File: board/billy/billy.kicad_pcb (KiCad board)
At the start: 2 copper layers, 70 x 50 mm, 82 parts, among them J1 Screw_Terminal_01x02, J10 Screw_Terminal_01x02, J11 Screw_Terminal_01x03, J12 USB_B_Micro, J2 Conn_01x06, J3 Screw_Terminal_01x02, J4 Screw_Terminal_01x02, J5 Conn_01x02, J6 Conn_01x03, J7 Screw_Terminal_01x06, Q1 AO3401A, Q2 AO3401A, Q4 AO3400A, Q6 AO3400A, Q7 AO3400A, SW1 TS-1088-AR02016, U1 ESP32-S3-WROOM-1, U2 DRV8833PWPR, U3 MAX98357A, U4 DRV8833PWPR, U5 LTC4412, U6 AP63203WU, U7 USBLC6-2SC6

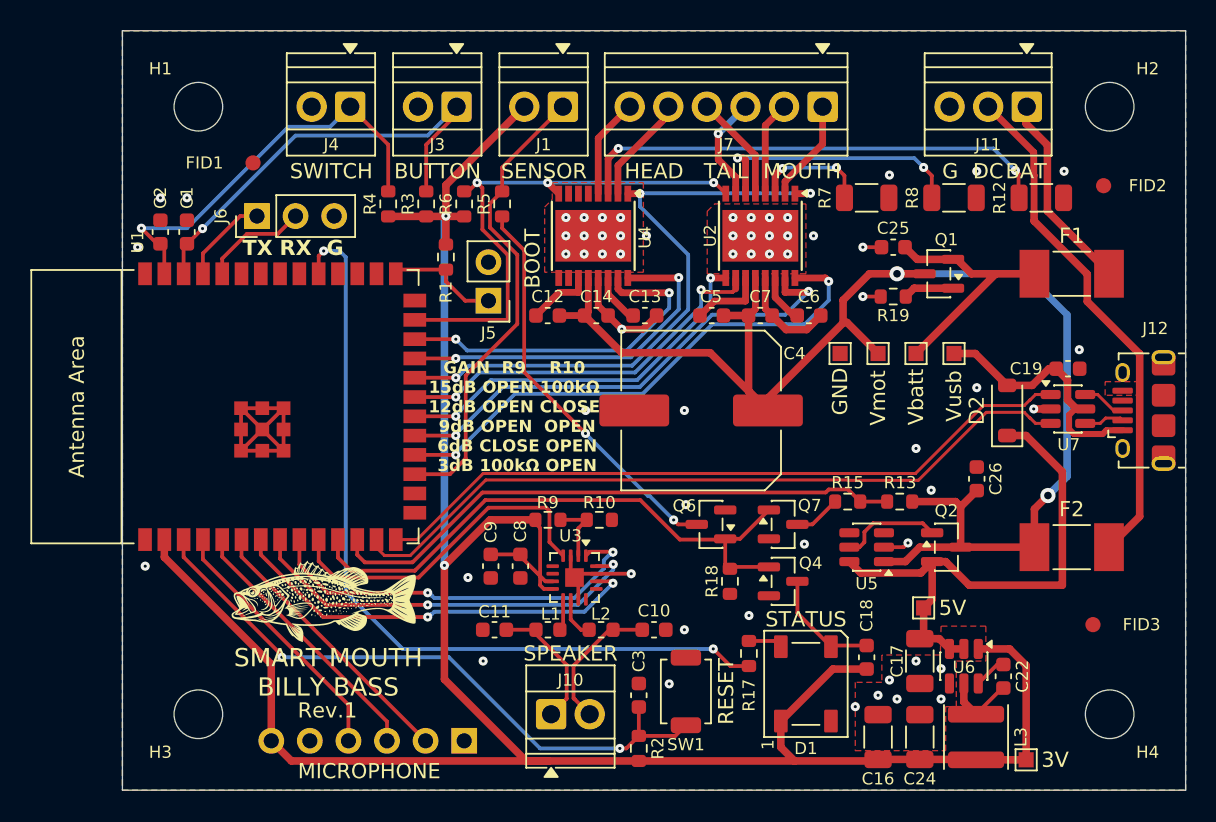
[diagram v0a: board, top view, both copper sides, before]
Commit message: Split rev.1's DRV8833 nSLEEP/nFAULT per chip for independent motor group control
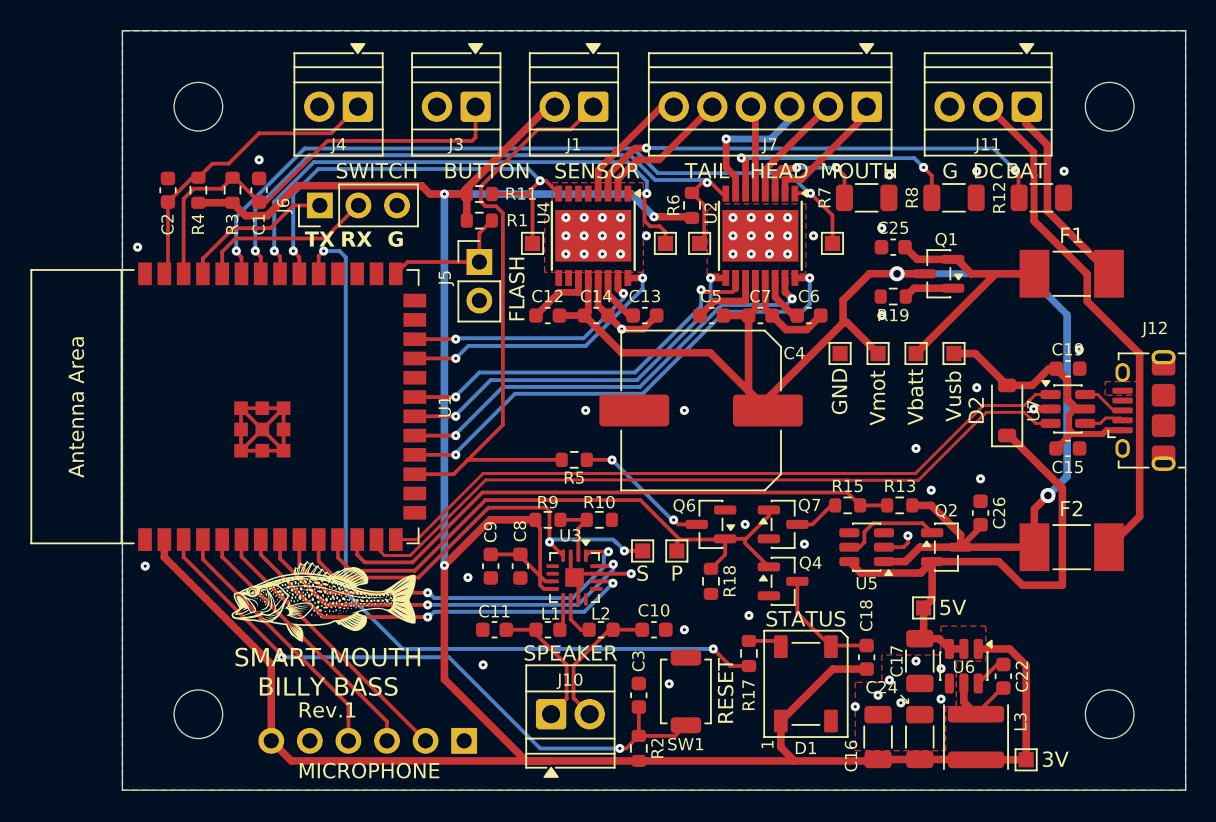
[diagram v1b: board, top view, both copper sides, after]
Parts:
- removed FID1, FID2, FID3: Fiducial_1mm_Mask2mm, Fiducial:Fiducial_1mm_Mask2mm
- added C15: 1u, Capacitor_SMD:C_0603_1608Metric, F.Cu at (212.2, 77.5)
- added R11: 10k, Resistor_SMD:R_0603_1608Metric, F.Cu at (173.5, 60.8)
- added TP10: TestPoint, TestPoint:TestPoint_Pad_1.0x1.0mm, F.Cu at (186.5, 84.2)
- added TP11: TestPoint, TestPoint:TestPoint_Pad_1.0x1.0mm, F.Cu at (185.8, 64.0)
- added TP12: TestPoint, TestPoint:TestPoint_Pad_1.0x1.0mm, F.Cu at (177.0, 64.0)
- added TP7: TestPoint, TestPoint:TestPoint_Pad_1.0x1.0mm, F.Cu at (196.8, 64.0)
- added TP8: TestPoint, TestPoint:TestPoint_Pad_1.0x1.0mm, F.Cu at (188.0, 64.0)
- added TP9: TestPoint, TestPoint:TestPoint_Pad_1.0x1.0mm, F.Cu at (184.2, 84.2)
- moved R5 17.5 mm to (179.8, 78.2), turned to 0 degrees
- moved R6 15.0 mm to (187.5, 61.5)
- moved R3 12.8 mm to (157.2, 60.5)
- moved R4 12.5 mm to (155.0, 60.5)
- moved C1 5.49 mm to (159.0, 60.5)
- moved J6 4.20 mm to (163.0, 61.5)
- moved R1 3.26 mm to (173.5, 62.5), turned to 0 degrees
- moved J7 2.90 mm to (199.0, 55.0)
- moved C2 2.80 mm to (153.0, 60.5)
- moved J5 2.62 mm to (173.5, 65.2), turned to 0 degrees
- moved C26 2.26 mm to (206.5, 81.8)
- moved J1 2.00 mm to (181.0, 55.0)
- moved J3 1.25 mm to (173.2, 55.0)
- moved R18 1.25 mm to (188.8, 86.2)
- moved J4 0.50 mm to (165.5, 55.0)
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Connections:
- net Vbatt renamed /Vbatt
- R6 pad 2: GPIO48 -> GPIO41
- U2 pad 1: GPIO14 -> GPIO42
- U2 pad 8: GPIO48 -> GPIO41
- U4 pad 1: GPIO14 -> GPIO40
- U4 pad 8: GPIO48 -> GPIO39
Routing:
- net GPIO42: track 0.00 -> 49.7 mm, vias 0 -> 2
- net GPIO41: track 0.00 -> 42.5 mm, vias 0 -> 2
- net GPIO14: track 41.9 -> 0.00 mm, vias 3 -> 0
- net GPIO40: track 0.00 -> 37.4 mm, vias 0 -> 2
- net GPIO48: track 34.5 -> 0.00 mm, vias 3 -> 0
- net GPIO39: track 0.00 -> 31.2 mm, vias 0 -> 2
- net +3.3V: track 159.0 -> 189.8 mm, vias 2 -> 3
- net Net-(Q6-D): track 26.4 -> 9.00 mm
- net GPIO9: track 30.7 -> 39.6 mm
- net GPIO1: track 26.8 -> 19.6 mm, vias 1 -> 0
- net GPIO47: track 23.4 -> 16.4 mm
- net GPIO17: track 22.4 -> 28.9 mm, vias 0 -> 2
- net GPIO21: track 24.2 -> 18.6 mm
- net U0RX: track 6.99 -> 11.6 mm
- net U0TX: track 5.92 -> 10.1 mm
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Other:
- board text added: "FLASH"
- board text added: "P"
- board text added: "S"
- board text removed: "BOOT"
- board text removed: "GAIN R9 R10 15dB OPEN 100kΩ 12dB OPEN CLOSE 9dB OPEN OPEN 6dB CLOSE OPEN 3dB 100kΩ OPEN"

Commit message: Split motor-rail bulk cap into two 220uF units, add solder-jumper Vmot->BUCK_IN bypass option
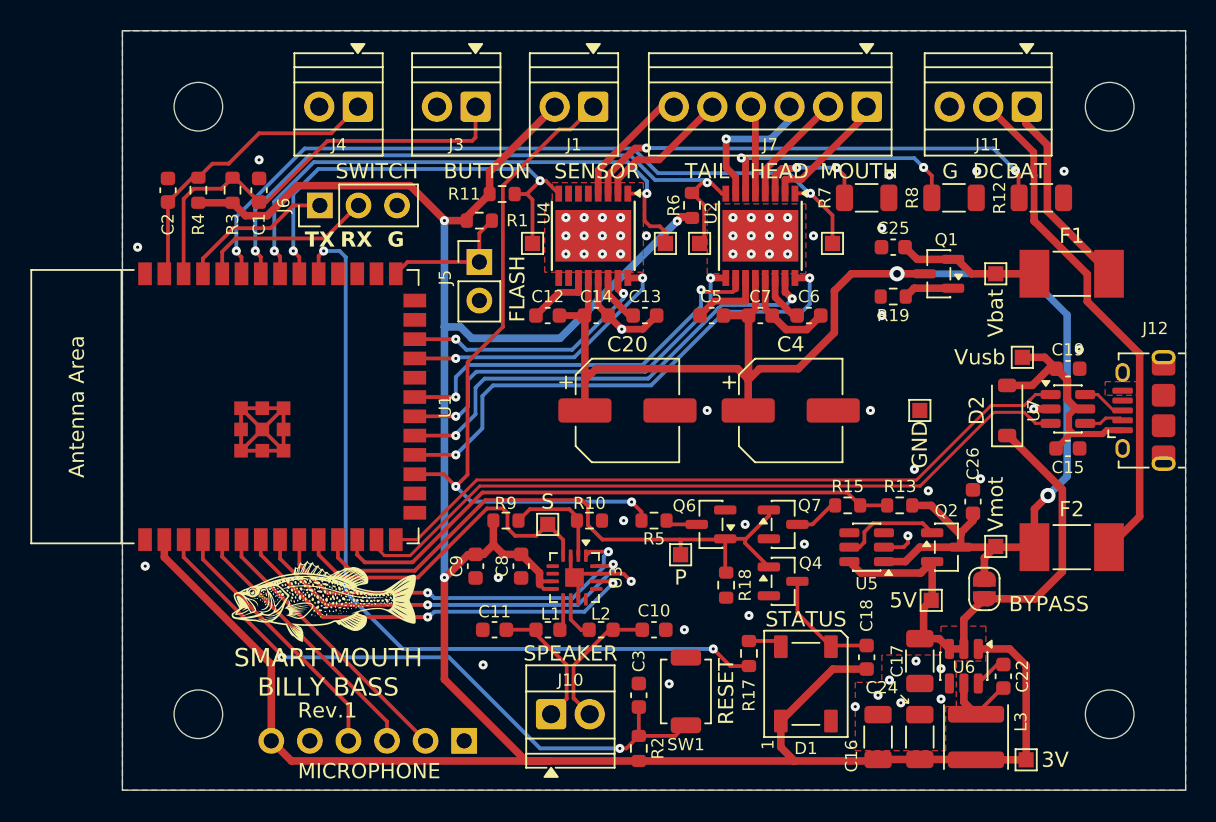
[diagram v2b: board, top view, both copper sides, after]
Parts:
- added C20: 220u, Capacitor_SMD:CP_Elec_6.3x5.9, F.Cu at (183.2, 75.0)
- added JP1: SolderJumper_2_Open, Jumper:SolderJumper-2_P1.3mm_Open_RoundedPad1.0x1.5mm, F.Cu at (206.8, 86.8)
- C4: value 1000u -> 220u; footprint Capacitor_SMD:C_Elec_10x10.2 -> Capacitor_SMD:CP_Elec_6.3x5.9
- moved TP1 14.9 mm to (207.5, 84.0)
- moved TP5 7.42 mm to (207.5, 66.0)
- moved R5 6.60 mm to (185.0, 82.2)
- moved TP9 6.49 mm to (178.0, 82.5)
- moved TP3 6.45 mm to (202.5, 75.0)
- moved C4 5.90 mm to (194.0, 75.0), turned to 0 degrees
- moved TP6 4.51 mm to (209.2, 71.5)
- moved R9 2.77 mm to (175.2, 82.2)
- moved R11 1.50 mm to (175.0, 60.8)
- moved R18 1.03 mm to (189.8, 86.5)
- moved C9 1.00 mm to (173.2, 85.2)
- moved C26 0.90 mm to (206.0, 81.0)
- moved TP4 0.71 mm to (203.2, 87.5)
- moved R10 0.65 mm to (180.8, 82.2)
- moved TP10 0.35 mm to (186.8, 84.5)
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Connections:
- net /Vbatt renamed /Vbat
- net BUCK_IN renamed Net-(D2-K)
- net Vusb renamed /Vusb
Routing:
- net /Vbat: track 16.4 -> 8.98 mm
- net Net-(Q6-D): track 9.00 -> 1.74 mm, vias 2 -> 0
- net GPIO17: track 28.9 -> 22.7 mm, vias 2 -> 0
- net GPIO9: track 39.6 -> 45.7 mm, vias 0 -> 2
- net +3.3V: track 189.8 -> 187.0 mm
- net Net-(U3-GAIN_SLOT): track 4.33 -> 6.52 mm
- net Vmot: track 94.0 -> 96.0 mm
- net /Vusb: track 19.3 -> 17.5 mm
- net GPIO39: track 31.2 -> 29.7 mm
- net GPIO10: track 32.9 -> 34.1 mm
- net GPIO11: track 30.3 -> 31.3 mm
- net GPIO12: track 25.4 -> 26.4 mm
- net GPIO13: track 25.6 -> 26.3 mm
- net GPIO18: track 39.0 -> 39.7 mm
- net GPIO47: track 16.4 -> 17.0 mm
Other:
- board text added: "BYPASS"
- board text added: "Vbat"
- board text removed: "Vbatt"

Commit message: Final prep of rev.1 board
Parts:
- removed TP1, TP4: TestPoint, TestPoint:TestPoint_Pad_1.0x1.0mm
- TP3: footprint TestPoint:TestPoint_Pad_1.0x1.0mm -> TestPoint:TestPoint_Keystone_5010-5014_Multipurpose
- moved SW1 33.6 mm to (154.0, 88.0), turned to 0 degrees
- moved R2 32.2 mm to (154.0, 85.5), turned to 0 degrees
- moved C3 30.2 mm to (154.0, 90.5), turned to 0 degrees
- moved TP2 7.32 mm to (210.5, 90.8)
- moved R17 4.05 mm to (187.7, 92.8)
- moved C18 3.71 mm to (195.7, 92.8)
- moved TP9 3.66 mm to (174.4, 83.4)
- moved D1 3.35 mm to (191.7, 92.8)
- moved R9 2.56 mm to (177.8, 82.5)
- moved TP6 1.75 mm to (207.5, 71.5)
- moved C26 1.42 mm to (204.6, 81.2), turned to 0 degrees
- moved G*** 1.25 mm to (164.5, 87.5)
- moved R6 1.25 mm to (186.5, 60.8), turned to 0 degrees
- moved TP10 1.15 mm to (185.6, 84.5)
- moved TP3 1.00 mm to (201.5, 75.0)
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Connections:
- net /J_N renamed Net-(J12-D-)
- net /J_P renamed Net-(J12-D+)
- net /Vbat renamed +BATT
- net /Vusb renamed VBUS
- net Net-(D2-K) renamed Vdrive
- net U_N renamed USB_D_N
- net U_P renamed USB_D_P
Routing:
- net EN: track 42.0 -> 11.1 mm, vias 2 -> 0
- net GND: track 41.8 -> 35.7 mm, vias 59 -> 60
- net GPIO38: track 53.9 -> 51.0 mm
- net Net-(U3-GAIN_SLOT): track 6.52 -> 3.68 mm
- net +3.3V: track 187.0 -> 189.1 mm
- net GPIO18: track 39.7 -> 41.0 mm
- net GPIO2: track 29.0 -> 30.3 mm
- net Net-(J11-Pin_2): track 34.0 -> 34.9 mm
- net Vdrive: track 34.4 -> 35.3 mm
- net Net-(U6-BST): track 2.17 -> 3.02 mm
- net Net-(D1-DIN): track 2.26 -> 3.02 mm
- net VBUS: track 17.5 -> 16.7 mm
- net GPIO40: track 37.4 -> 36.7 mm
- net Net-(U6-SW): track 4.80 -> 5.46 mm
- net Net-(Q1-G): track 3.34 -> 3.94 mm
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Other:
- board text added: "3.3V"
- board text added: "BATT"
- board text added: "EN"
- board text added: "GAIN CTRL"
- board text added: "GND DC BAT"
- board text added: "MODE"
- board text added: "OK"
- board text added: "PERIPH"
- board text added: "SD"
- board text added: "TAIL HEAD MOUTH"
- board text added: "VBUS"
- board text added: "VDRIVE"
- board text added: "VMOT"
- board text removed: "3V"
- board text removed: "5V"
- board text removed: "BAT"
- board text removed: "DC"
- board text removed: "HEAD"
- board text removed: "MOUTH"
- board text removed: "P"
- board text removed: "S"
- board text removed: "TAIL"
- board text removed: "Vbat"
- board text removed: "Vmot"
- board text removed: "Vusb"

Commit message: Rev 2 board updates
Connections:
- U4 pad 6: unconnected-(U4-BISEN-Pad6) -> GND
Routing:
- net GND: track 35.7 -> 37.2 mm, vias 60 -> 61
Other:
- board text added: "Rev.2"
- board text removed: "Rev.1"

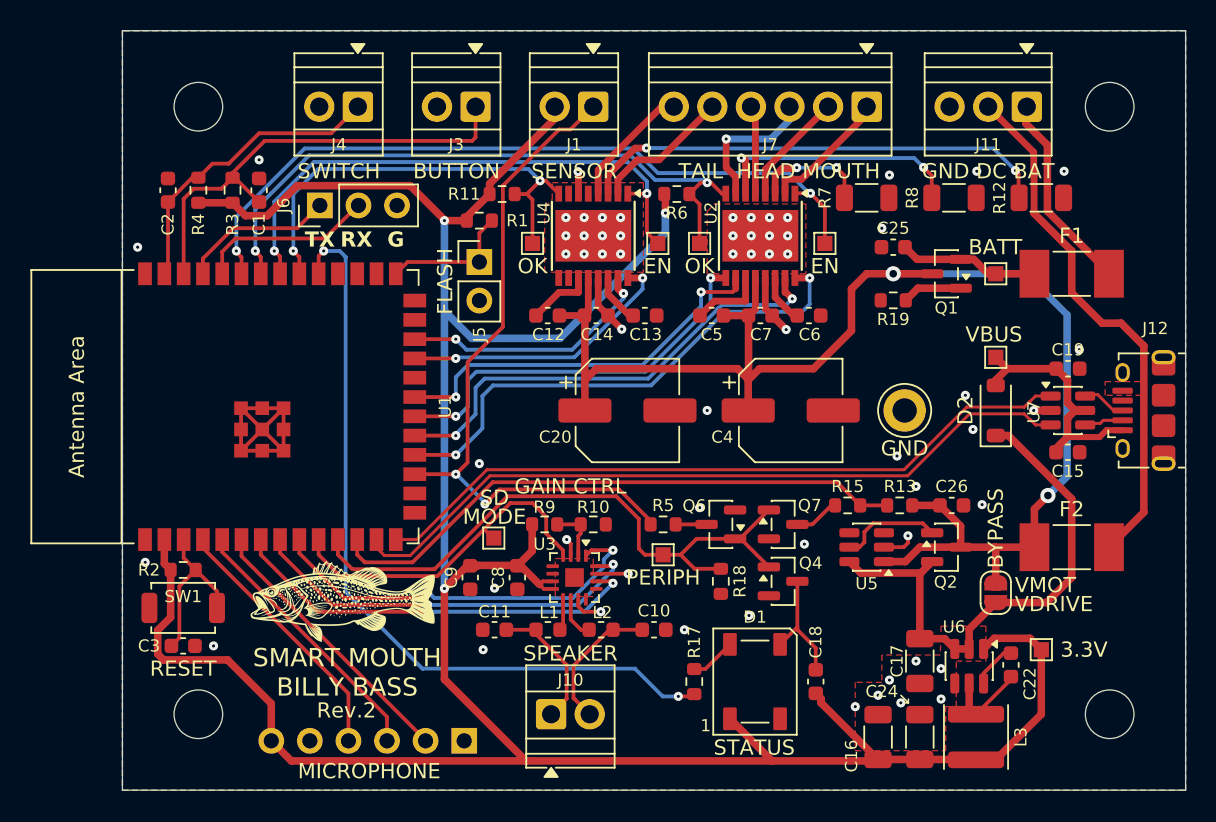
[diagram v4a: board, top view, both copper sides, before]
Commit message: Add motor output snubber caps (C27-C29) across mouth/head/tail for EMI suppression
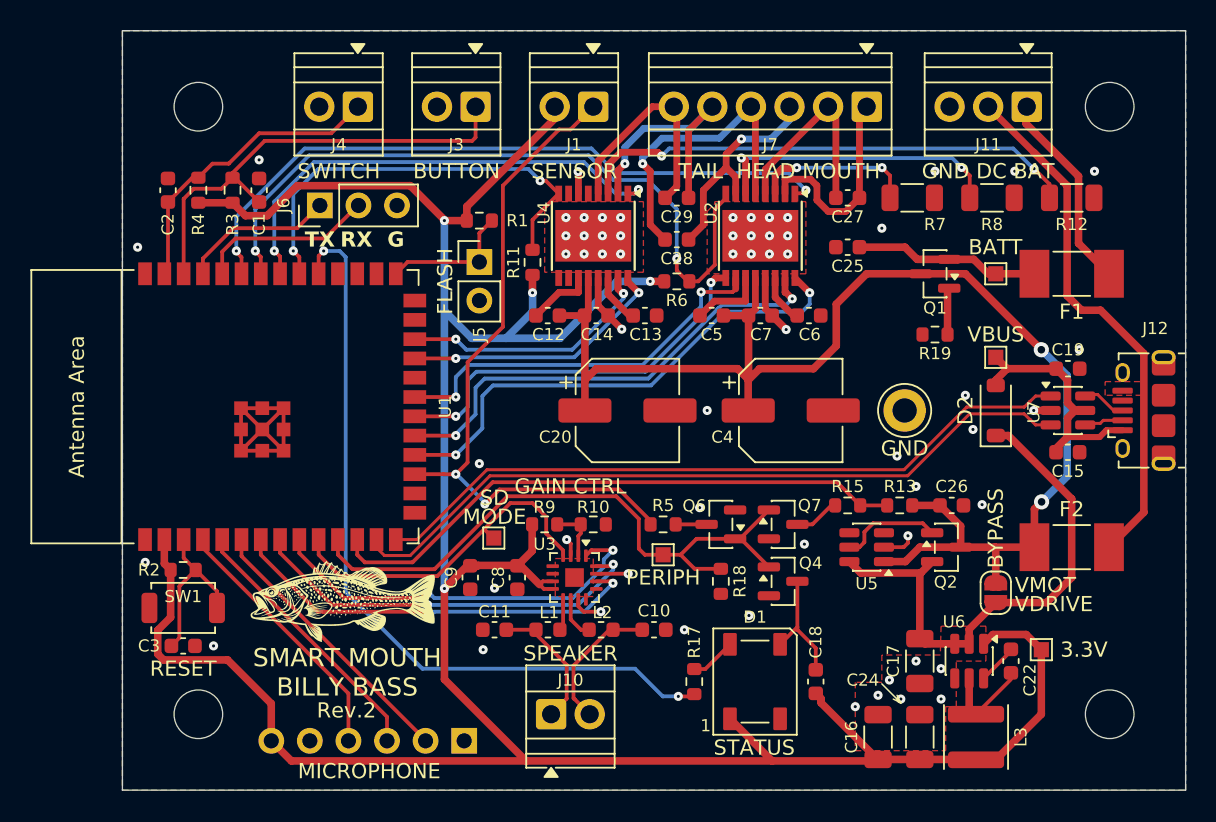
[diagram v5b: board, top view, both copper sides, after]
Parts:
- removed TP11, TP12, TP7, TP8: TestPoint, TestPoint:TestPoint_Pad_1.0x1.0mm
- added C27: 100n, Capacitor_SMD:C_0603_1608Metric, F.Cu at (197.8, 61.0)
- added C28: 100n, Capacitor_SMD:C_0603_1608Metric, F.Cu at (186.5, 63.8)
- added C29: 100n, Capacitor_SMD:C_0603_1608Metric, F.Cu at (186.5, 61.0)
- moved R6 5.75 mm to (186.5, 66.5)
- moved R11 4.92 mm to (177.0, 65.2), turned to 90 degrees
- moved R19 3.55 mm to (203.5, 70.0)
- moved C25 3.00 mm to (197.8, 64.2)
- moved R7 3.00 mm to (202.0, 61.0)
- moved R8 2.50 mm to (207.2, 61.0)
- moved R12 2.00 mm to (212.5, 61.0)
- moved Q1 0.75 mm to (203.5, 66.0)
- moved U6 0.34 mm to (205.8, 91.5)
- moved C22 0.25 mm to (208.5, 91.5)
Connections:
- net Net-(J7-Pin_1) renamed /M_MOUTH1
- net Net-(J7-Pin_2) renamed /M_MOUTH2
- net Net-(J7-Pin_3) renamed /M_HEAD1
- net Net-(J7-Pin_4) renamed /M_HEAD2
- net Net-(J7-Pin_5) renamed /M_TAIL1
- net Net-(J7-Pin_6) renamed /M_TAIL2
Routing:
- net /M_HEAD2: track 5.43 -> 20.0 mm, vias 0 -> 1
- net /M_TAIL1: track 9.14 -> 16.8 mm, vias 0 -> 1
- net /M_TAIL2: track 8.25 -> 15.0 mm
- net /M_MOUTH2: track 7.44 -> 13.7 mm
- net /M_MOUTH1: track 8.10 -> 13.9 mm
- net /M_HEAD1: track 9.43 -> 14.6 mm
- net GPIO40: track 36.7 -> 31.7 mm
- net Vmot: track 95.5 -> 90.6 mm
- net GPIO41: track 42.9 -> 47.4 mm
- net GPIO42: track 49.5 -> 45.2 mm
- net Net-(U2-AISEN): track 7.67 -> 10.7 mm
- net Net-(U4-AISEN): track 30.6 -> 33.5 mm
- net Net-(U2-BISEN): track 17.0 -> 19.5 mm
- net +BATT: track 9.48 -> 11.7 mm
- net +3.3V: track 189.1 -> 190.2 mm, vias 3 -> 4
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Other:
- board text removed: "EN"
- board text removed: "OK"

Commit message: Remove JP1 debug solder jumper and reroute Vmot direct to motor caps
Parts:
- removed JP1: SolderJumper_2_Open, Jumper:SolderJumper-2_P1.3mm_Open_RoundedPad1.0x1.5mm
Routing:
- net Vmot: track 90.6 -> 79.1 mm
- net Vdrive: track 34.8 -> 28.2 mm, vias 0 -> 2
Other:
- board text removed: "BYPASS"
- board text removed: "VDRIVE"
- board text removed: "VMOT"
